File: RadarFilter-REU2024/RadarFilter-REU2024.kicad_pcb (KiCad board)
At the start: 2 copper layers, 87.4 x 50 mm, 32 parts, among them J1 73099-0, J2 73099-0, J3 73099-0, J4 Conn_01x04_Pin, J5 Conn_01x04_Pin, J6 CONSMA002, J7 CONSMA002, J8 CONSMA002, J9 CONSMA002, U5 ADA4807-2ARM, U6 ADA4807-2ARM

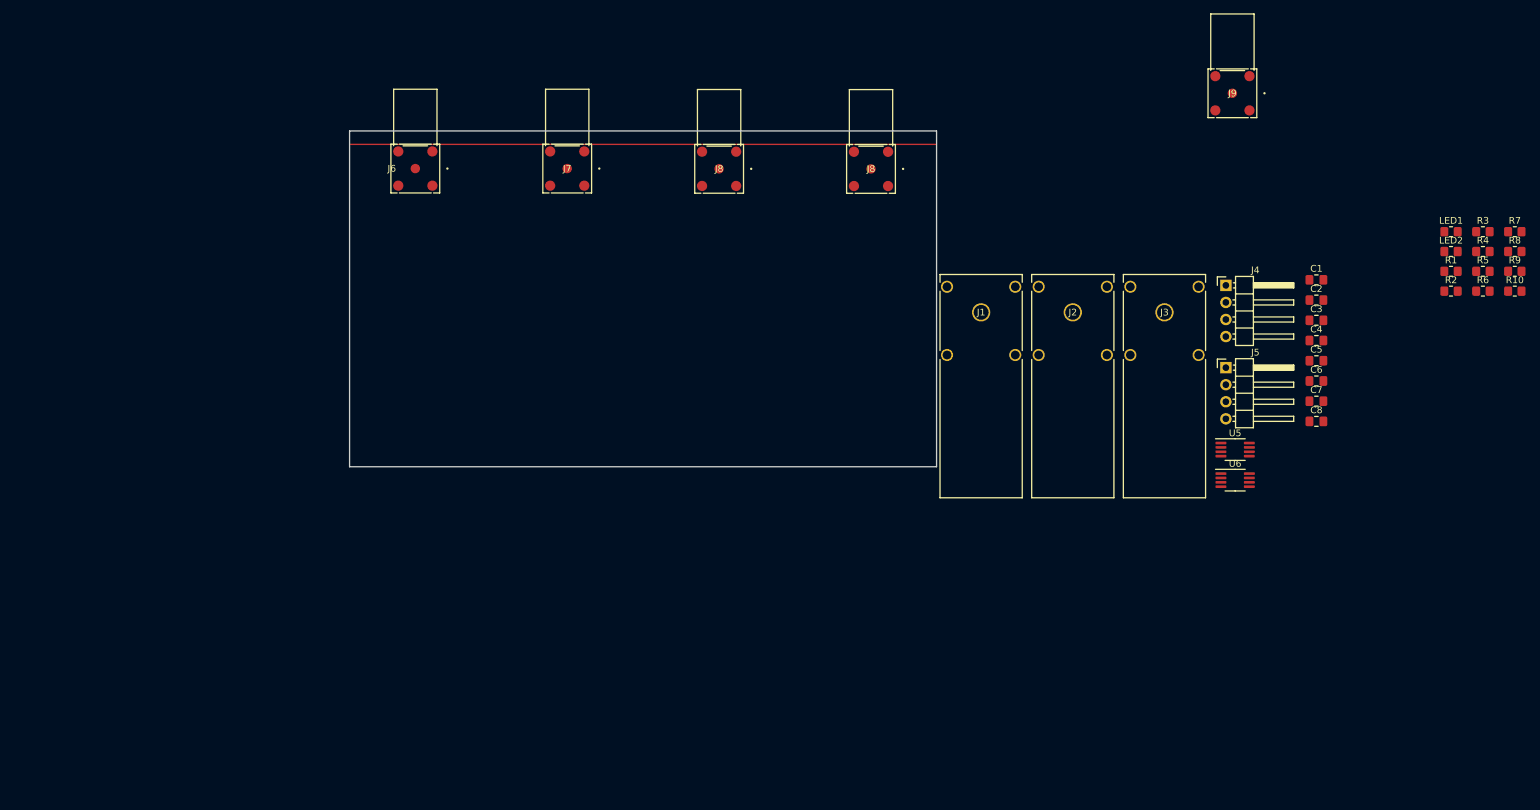
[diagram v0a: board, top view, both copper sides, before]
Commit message: changed sma connector footprint, added ground pour to pcb layout
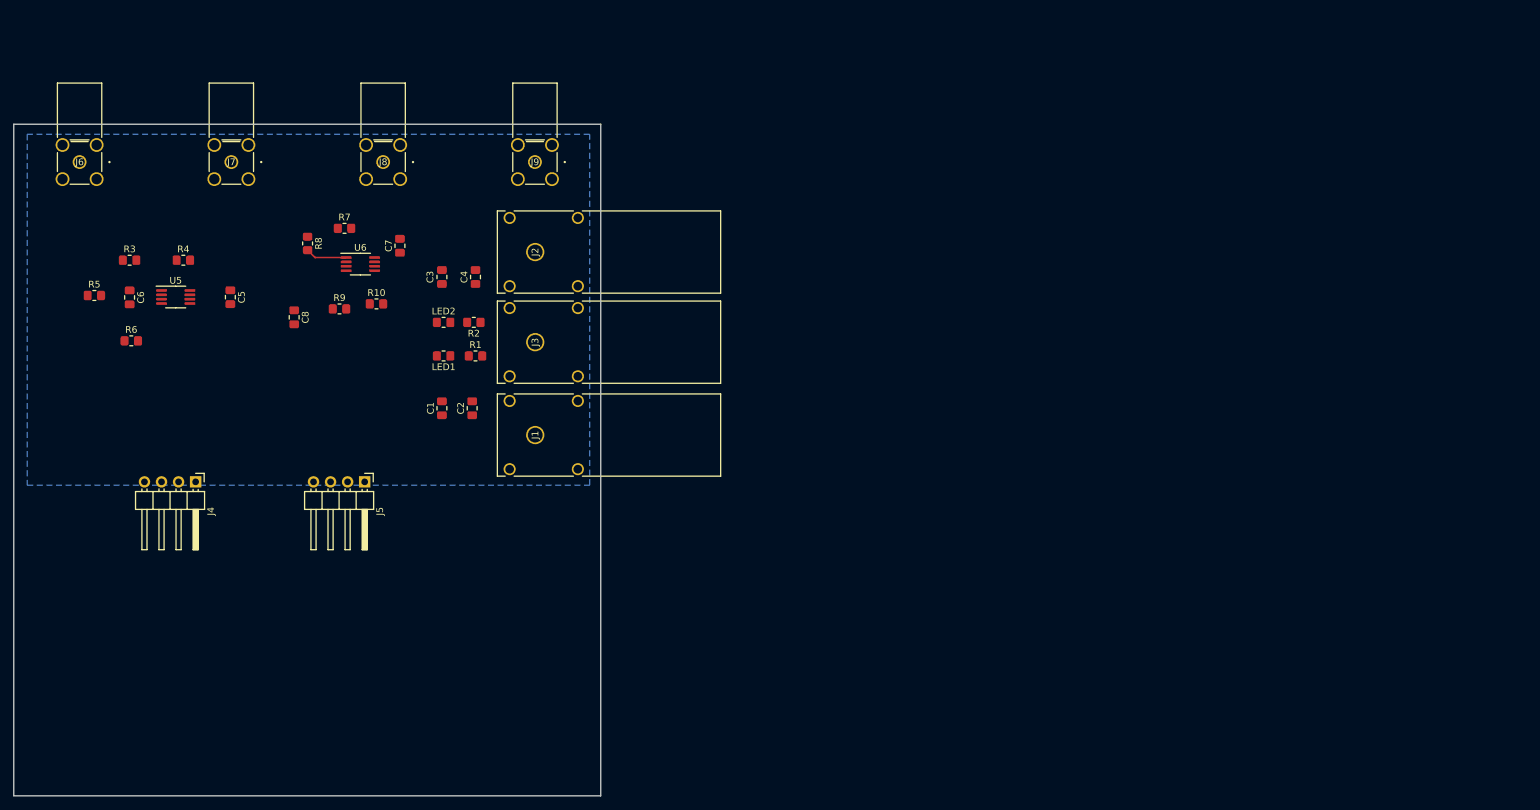
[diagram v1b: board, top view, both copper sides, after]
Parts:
- removed the J8 at (155.0, 56.6)
- removed the J8 at (177.6, 56.6)
- added J8: CONSMA002, 0731000115:COAX4GND_731000115_MOL, F.Cu at (105.0, 55.6)
- J6, J7, J9: footprint CONSMA002:COAX4_CONSMA002_TEC -> 0731000115:COAX4GND_731000115_MOL
- moved R5 206.8 mm to (62.0, 75.5)
- moved R3 201.5 mm to (67.2, 70.2)
- moved R6 201.4 mm to (67.5, 82.2)
- moved R4 193.5 mm to (75.2, 70.2)
- moved R8 179.8 mm to (93.8, 67.8), turned to -90 degrees
- moved C6 177.1 mm to (67.2, 75.8), turned to -90 degrees
- moved R9 175.1 mm to (98.5, 77.5)
- moved R7 174.3 mm to (99.2, 65.5)
- moved R10 169.5 mm to (104.0, 76.8)
- moved C5 162.0 mm to (82.2, 75.8), turned to -90 degrees
- moved U5 159.4 mm to (74.1, 75.7)
- moved J4 156.2 mm to (77.1, 103.2), turned to -90 degrees
- moved C8 153.0 mm to (91.8, 78.8), turned to -90 degrees
- moved LED1 151.1 mm to (114.0, 84.5), turned to 180 degrees
- moved LED2 150.4 mm to (114.0, 79.5)
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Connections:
- net BNC1I renamed SMA1I
- net BNC1Q renamed SMA1Q
- net BNC2I renamed SMA2I
- net BNC2Q renamed SMA2Q
- J1 pad 2: (no net) -> GND
- J1 pad 3: (no net) -> GND
- J1 pad 4: (no net) -> GND
- J1 pad 5: (no net) -> GND
- J2 pad 2: (no net) -> GND
- J2 pad 3: (no net) -> GND
- J2 pad 4: (no net) -> GND
- J2 pad 5: (no net) -> GND
- J3 pad 2: (no net) -> GND
- J3 pad 3: (no net) -> GND
- J3 pad 4: (no net) -> GND
- J3 pad 5: (no net) -> GND
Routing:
- net SMA2I: track 0.00 -> 6.21 mm
- added copper zone on B.Cu, net GND
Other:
- board size 87.4 x 50 mm -> 87.4 x 100 mm

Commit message: pcb layout iteration complete
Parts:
- moved R7 21.7 mm to (84.3, 81.2), turned to 90 degrees
- moved R4 17.5 mm to (57.8, 71.2), turned to 90 degrees
- moved R5 16.8 mm to (77.8, 81.2), turned to 90 degrees
- moved C5 15.4 mm to (67.5, 71.2), turned to 90 degrees
- moved R6 15.1 mm to (77.8, 71.2), turned to 90 degrees
- moved R3 14.5 mm to (57.8, 81.2), turned to 90 degrees
- moved C7 13.2 mm to (94.7, 71.2)
- moved R8 10.1 mm to (84.3, 71.2), turned to 90 degrees
- moved U6 9.12 mm to (94.3, 76.2)
- moved C2 8.13 mm to (116.8, 100.3)
- moved C3 7.24 mm to (116.8, 66.2)
- moved R9 6.88 mm to (104.3, 81.2), turned to 90 degrees
- moved U5 6.36 mm to (67.8, 76.2)
- moved R10 5.52 mm to (104.3, 71.2), turned to 90 degrees
- moved J4 5.51 mm to (71.6, 103.2)
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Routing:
- net /V+: track 0.00 -> 208.8 mm, vias 0 -> 4
- net /V-: track 0.00 -> 143.2 mm, vias 0 -> 2
- net GND: track 0.00 -> 43.0 mm, vias 0 -> 11
- net SMA2Q: track 0.00 -> 39.2 mm
- net SMA2I: track 6.21 -> 40.7 mm
- net 2I: track 0.00 -> 30.0 mm
- net 1I: track 0.00 -> 29.2 mm
- net 1Q: track 0.00 -> 29.1 mm
- net 2Q: track 0.00 -> 29.0 mm
- net SMA1I: track 0.00 -> 26.5 mm
- net SMA1Q: track 0.00 -> 25.8 mm
- net Net-(U6B--): track 0.00 -> 16.5 mm
- net Net-(U5A--): track 0.00 -> 16.4 mm
- net Net-(U5B--): track 0.00 -> 16.3 mm
- net Net-(U6A--): track 0.00 -> 16.3 mm
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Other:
- board size 87.4 x 100 mm -> 87.4 x 57 mm

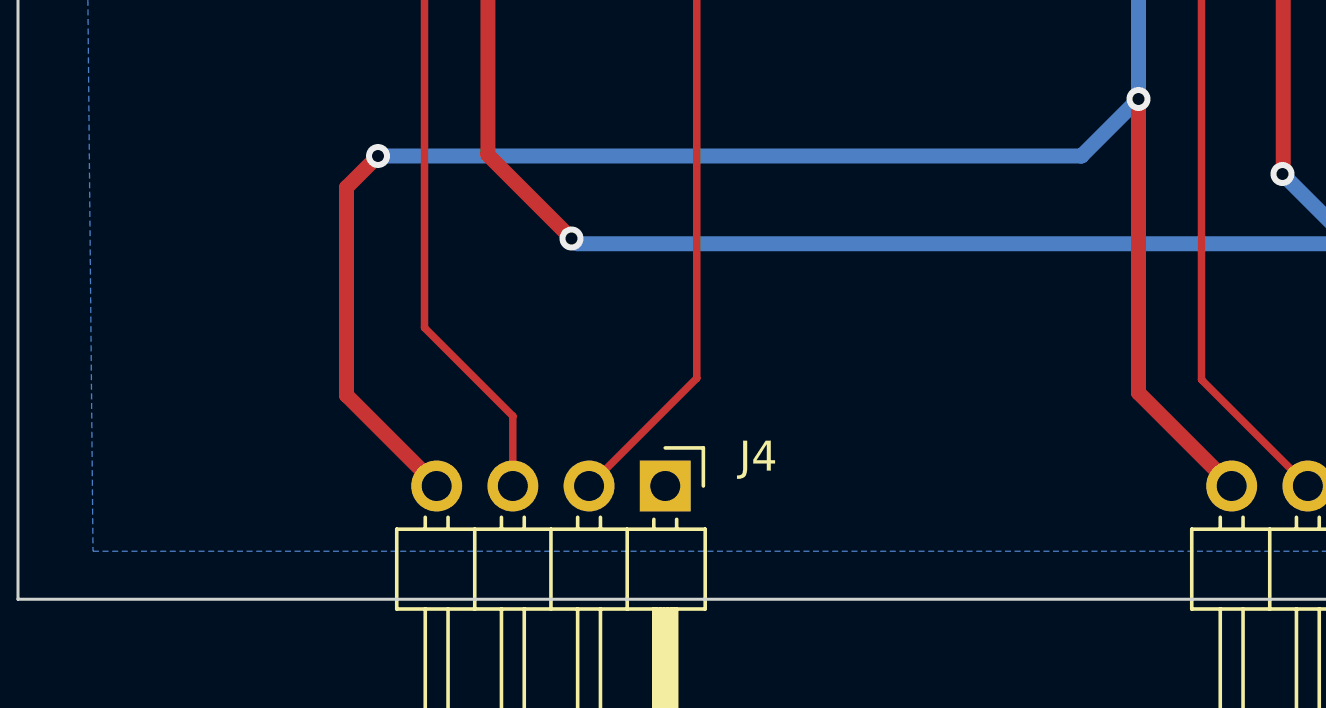
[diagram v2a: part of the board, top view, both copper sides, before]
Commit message: added bypass capacitors for KLC5 radar header pins
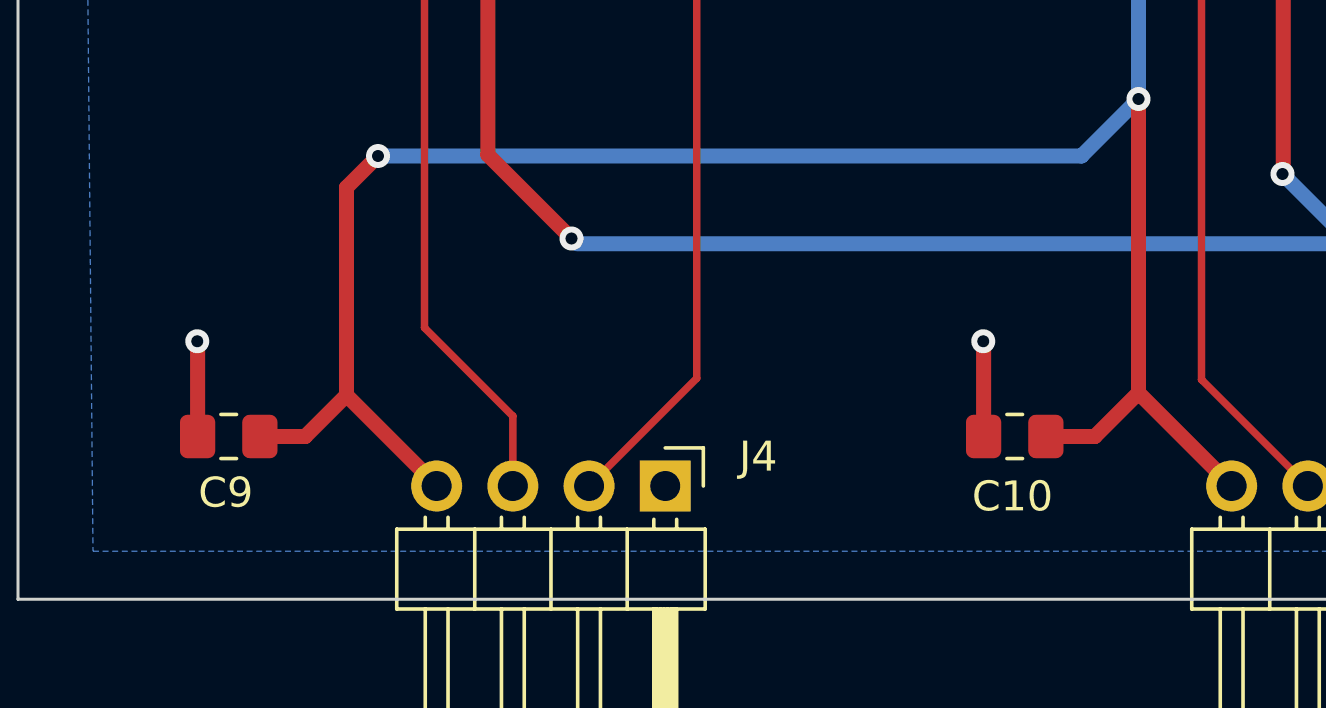
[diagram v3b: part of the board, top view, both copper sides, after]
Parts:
- added C10: 0.1uF, Capacitor_SMD:C_0805_2012Metric_Pad1.18x1.45mm_HandSolder, F.Cu at (83.2, 101.6)
- added C9: 0.1uF, Capacitor_SMD:C_0805_2012Metric_Pad1.18x1.45mm_HandSolder, F.Cu at (57.0, 101.6)
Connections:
- J1 pad 2: GND -> (no net)
- J1 pad 3: GND -> (no net)
- J1 pad 4: GND -> (no net)
- J1 pad 5: GND -> (no net)
- J2 pad 2: GND -> (no net)
- J2 pad 3: GND -> (no net)
- J2 pad 4: GND -> (no net)
- J2 pad 5: GND -> (no net)
- J3 pad 2: GND -> (no net)
- J3 pad 3: GND -> (no net)
- J3 pad 4: GND -> (no net)
- J3 pad 5: GND -> (no net)
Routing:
- net /V+: track 208.8 -> 215.9 mm
- net GND: track 43.0 -> 49.3 mm, vias 11 -> 13

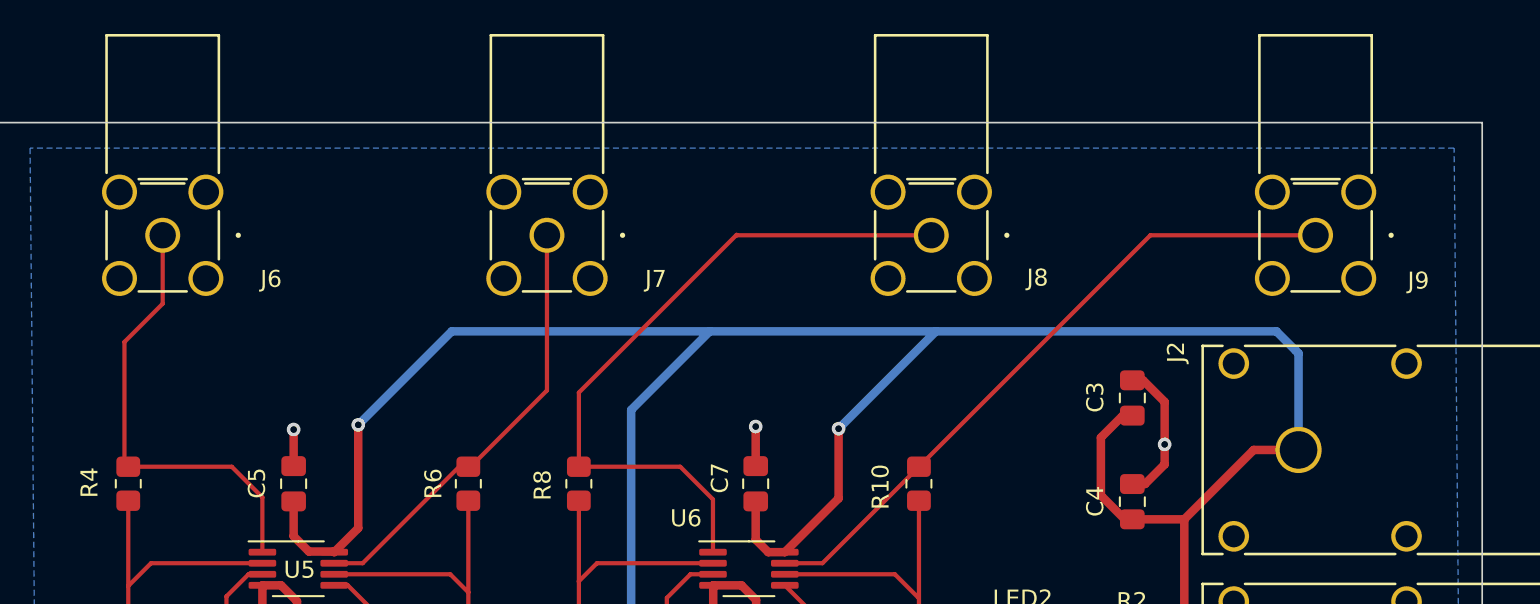
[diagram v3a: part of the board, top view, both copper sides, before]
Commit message: adjusted spacing of sma connectors and slight pcb trace modification
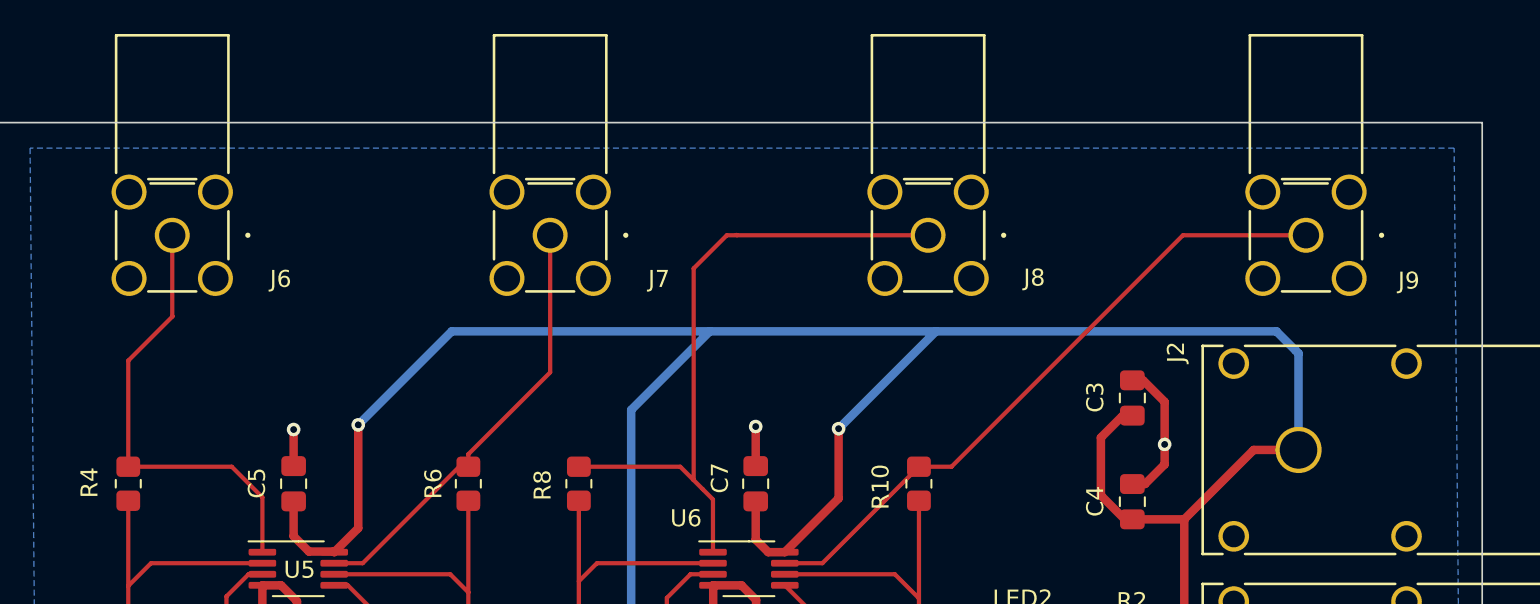
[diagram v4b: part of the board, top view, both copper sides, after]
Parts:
- moved J6 0.56 mm to (60.4, 56.6)
- moved J9 0.56 mm to (127.0, 56.6)
- moved J7 0.19 mm to (82.6, 56.6)
- moved J8 0.19 mm to (104.8, 56.6)
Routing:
- net SMA2I: track 40.7 -> 38.9 mm
- net SMA2Q: track 39.2 -> 38.6 mm
